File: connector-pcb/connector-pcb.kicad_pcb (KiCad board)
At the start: 2 copper layers, 79 x 43 mm, 39 parts, among them J1 MSO5000_LA, J2 IDC_HEADER_2x12, J3 IDC_HEADER_2x12, U1 MCP6002-xMS, U2 MCP6002-xMS

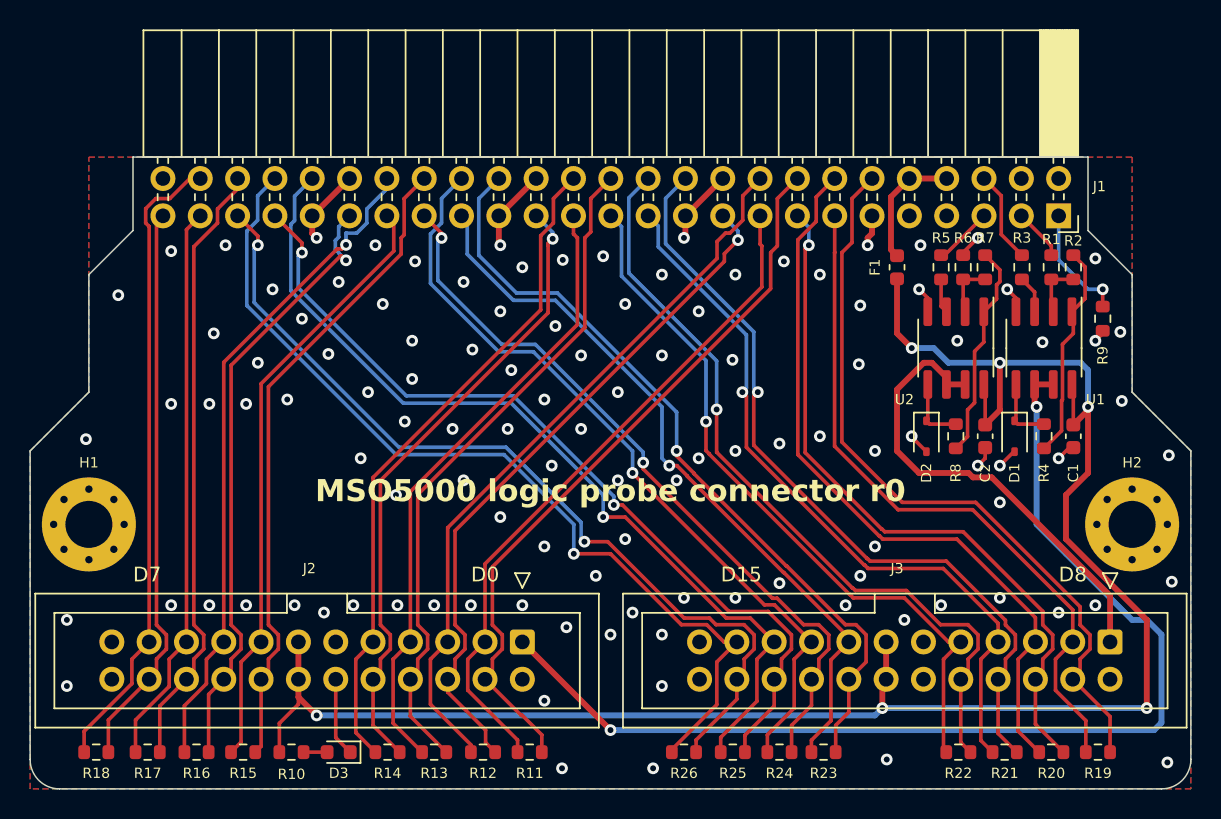
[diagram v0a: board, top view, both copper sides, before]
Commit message: Change connector PCB to 4 layer board, finalize probe board
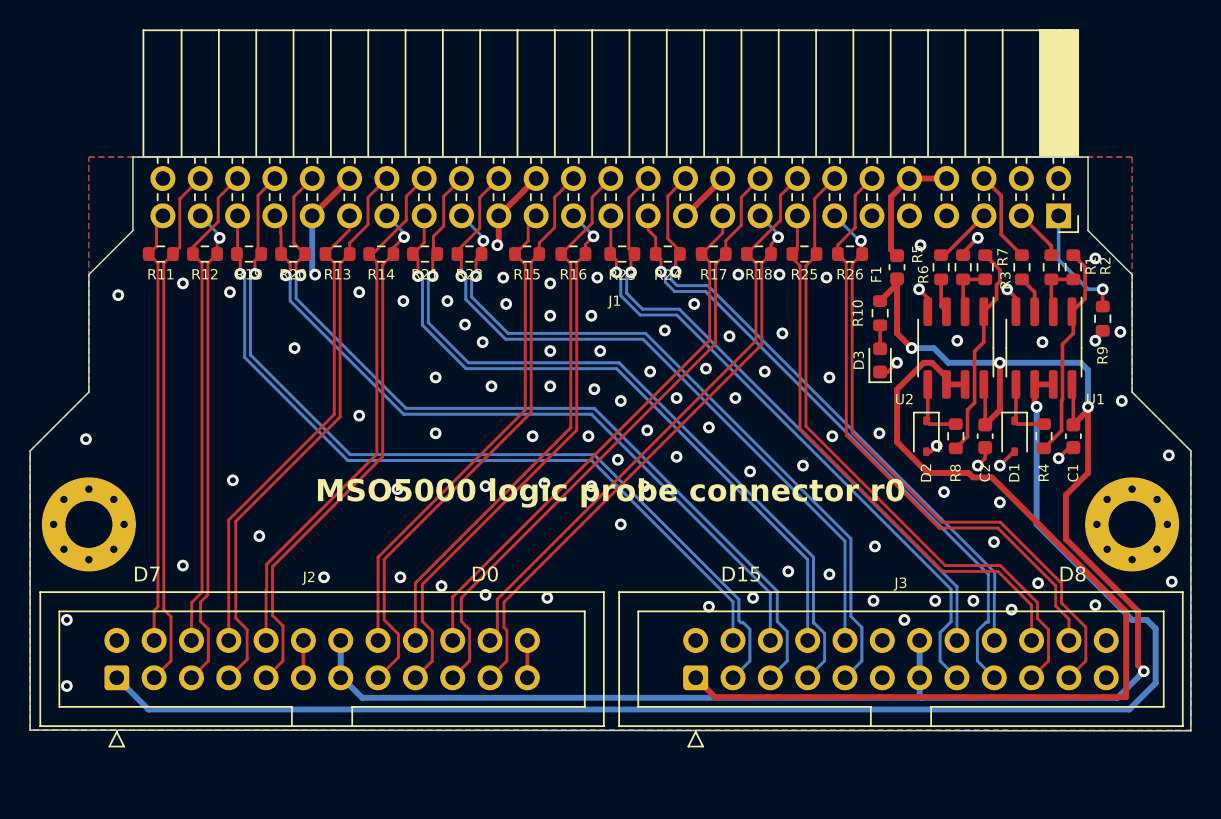
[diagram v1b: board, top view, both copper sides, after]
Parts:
- D1, D2: value 3.3V -> 3.3V 2%
- moved R19 67.0 mm to (74.9, 55.6), turned to 0 degrees
- moved R20 61.7 mm to (77.9, 55.6), turned to 0 degrees
- moved R18 56.4 mm to (109.6, 55.6), turned to 0 degrees
- moved R21 52.0 mm to (86.9, 55.6), turned to 0 degrees
- moved R17 51.3 mm to (106.5, 55.6), turned to 0 degrees
- moved R10 50.0 mm to (117.8, 59.6), turned to -90 degrees
- moved R22 47.5 mm to (89.9, 55.6), turned to 0 degrees
- moved D3 45.5 mm to (117.8, 62.8), turned to 90 degrees
- moved R16 42.5 mm to (97.0, 55.6), turned to 0 degrees
- moved R11 42.2 mm to (68.9, 55.6), turned to 0 degrees
- moved R15 39.0 mm to (93.8, 55.6), turned to 0 degrees
- moved R12 38.8 mm to (71.9, 55.6), turned to 0 degrees
- moved R23 36.6 mm to (100.3, 55.6)
- moved R26 35.7 mm to (115.8, 55.6), turned to 0 degrees
- moved R24 34.7 mm to (103.4, 55.6)
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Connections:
- J2 pad 10: /D3_N -> /D4_N
- J2 pad 15: /D4_P -> /D3_P
- J2 pad 16: /D4_N -> /D3_N
- J2 pad 17: /D5_P -> /D2_P
- J2 pad 18: /D5_N -> /D2_N
- J2 pad 19: /D6_P -> /D1_P
- J2 pad 20: /D6_N -> /D1_N
- J2 pad 21: /D7_P -> /D0_P
- J2 pad 22: /D7_N -> /D0_N
- J2 pad 3: /D0_P -> /D7_P
- J2 pad 4: /D0_N -> /D7_N
- J2 pad 5: /D1_P -> /D6_P
- J2 pad 6: /D1_N -> /D6_N
- J2 pad 7: /D2_P -> /D5_P
- J2 pad 8: /D2_N -> /D5_N
- J2 pad 9: /D3_P -> /D4_P
- J3 pad 10: /D11_N -> /D12_N
- J3 pad 15: /D12_P -> /D11_P
- J3 pad 16: /D12_N -> /D11_N
- J3 pad 17: /D13_P -> /D10_P
- J3 pad 18: /D13_N -> /D10_N
- J3 pad 19: /D14_P -> /D9_P
- J3 pad 20: /D14_N -> /D9_N
- J3 pad 21: /D15_P -> /D8_P
- J3 pad 22: /D15_N -> /D8_N
- J3 pad 3: /D8_P -> /D15_P
- J3 pad 4: /D8_N -> /D15_N
- J3 pad 5: /D9_P -> /D14_P
- J3 pad 6: /D9_N -> /D14_N
- J3 pad 7: /D10_P -> /D13_P
- J3 pad 8: /D10_N -> /D13_N
- J3 pad 9: /D11_P -> /D12_P
- R11 pad 1: /D0_N -> /D7_N
- R11 pad 2: /D0_P -> /D7_P
- R12 pad 1: /D1_N -> /D6_N
- R12 pad 2: /D1_P -> /D6_P
- R13 pad 1: /D2_N -> /D5_N
- R13 pad 2: /D2_P -> /D5_P
- R14 pad 1: /D3_N -> /D4_N
- R14 pad 2: /D3_P -> /D4_P
- R15 pad 1: /D4_N -> /D3_N
- R15 pad 2: /D4_P -> /D3_P
- R16 pad 1: /D5_N -> /D2_N
- R16 pad 2: /D5_P -> /D2_P
- R17 pad 1: /D6_N -> /D1_N
- R17 pad 2: /D6_P -> /D1_P
- R18 pad 1: /D7_N -> /D0_N
- R18 pad 2: /D7_P -> /D0_P
- R19 pad 1: /D8_N -> /D15_N
- R19 pad 2: /D8_P -> /D15_P
- R20 pad 1: /D9_N -> /D14_N
- R20 pad 2: /D9_P -> /D14_P
- R21 pad 1: /D10_N -> /D13_N
- R21 pad 2: /D10_P -> /D13_P
- R22 pad 1: /D11_N -> /D12_N
- R22 pad 2: /D11_P -> /D12_P
- R23 pad 1: /D12_N -> /D11_N
- R23 pad 2: /D12_P -> /D11_P
- R24 pad 1: /D13_N -> /D10_N
- R24 pad 2: /D13_P -> /D10_P
- R25 pad 1: /D14_N -> /D9_N
- R25 pad 2: /D14_P -> /D9_P
- R26 pad 1: /D15_N -> /D8_N
- R26 pad 2: /D15_P -> /D8_P
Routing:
- net /Vref_8_15_out: track 32.2 -> 65.9 mm
- net /Vref_0_7_out: track 74.6 -> 97.9 mm, vias 2 -> 1
- net /D10_N: track 53.8 -> 42.9 mm
- net +4V: track 127.8 -> 117.3 mm, vias 6 -> 4
- net /D9_N: track 48.3 -> 38.0 mm, vias 1 -> 0
- net /D11_N: track 53.3 -> 43.1 mm
- net /D8_N: track 51.4 -> 41.3 mm
- net /D1_N: track 47.0 -> 37.0 mm, vias 1 -> 0
- net /D5_N: track 42.3 -> 32.8 mm, vias 1 -> 0
- net /D0_N: track 50.1 -> 40.6 mm
- net /D3_N: track 43.3 -> 33.9 mm, vias 1 -> 0
- net /D7_N: track 38.6 -> 29.7 mm
- net /D2_N: track 46.3 -> 37.5 mm
- net /D6_N: track 41.8 -> 33.3 mm
- net /D14_N: track 58.8 -> 50.6 mm, vias 2 -> 1
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- added copper zone on In1.Cu, net GND
- added copper zone on In2.Cu, net GND
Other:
- board size 79 x 43 mm -> 79 x 39 mm
- copper layers 2 -> 4
- board text added: "Order selection:JLC7628, 1.6mm, 100Ohm diff. impedance"

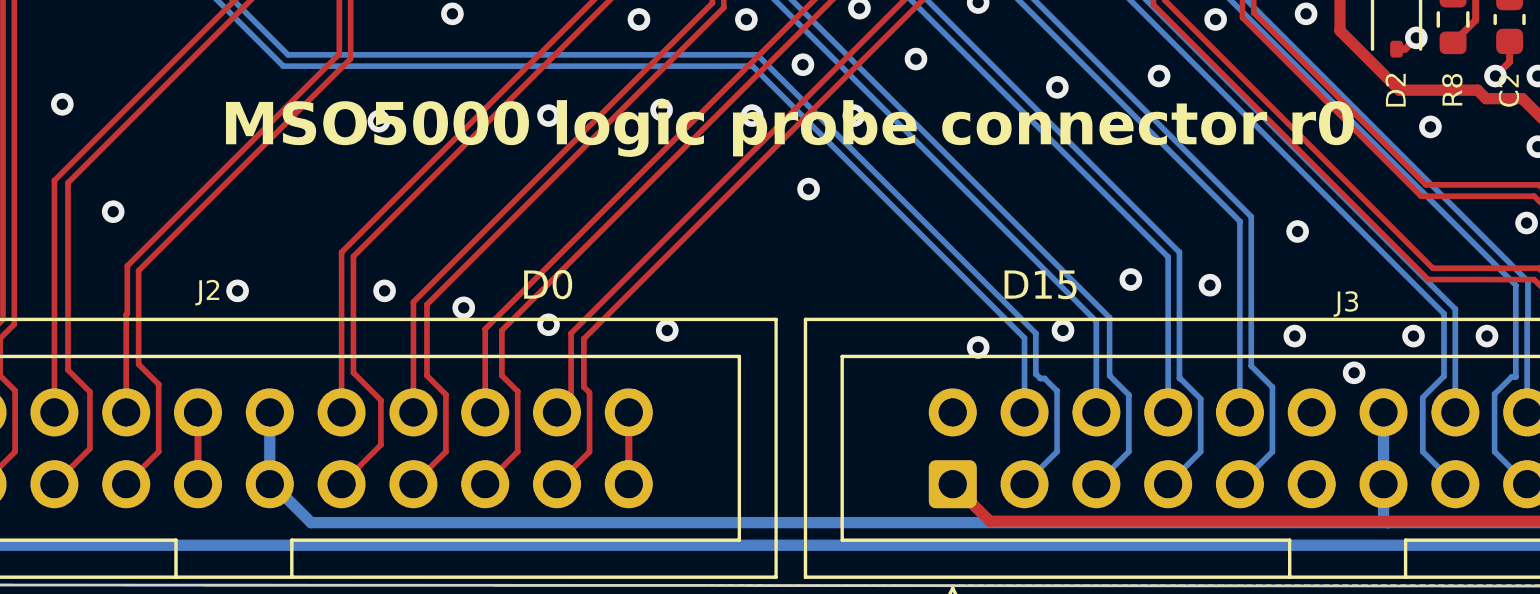
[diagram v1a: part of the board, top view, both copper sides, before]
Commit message: Add 3d model for 2x12 pin header (missing in kicad library), add readme
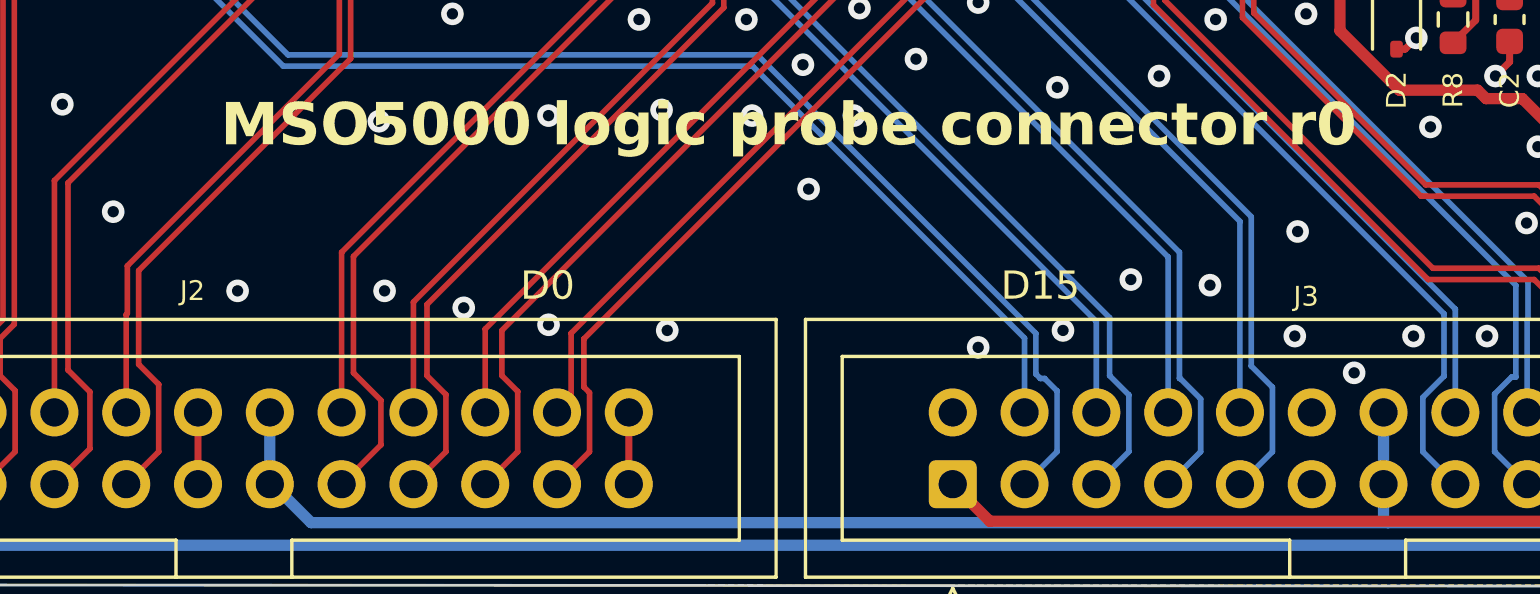
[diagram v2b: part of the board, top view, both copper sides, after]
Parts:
- J2, J3: footprint Connector_IDC:IDC-Header_2x12_P2.54mm_Vertical -> idc:IDC-Header_2x12_P2.54mm_Vertical
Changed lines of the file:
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@@
     (pad "20" thru_hole oval (at -2.54 22.86 270) (size 1.7 1.7) (drill 1) (layers "*.Cu" "*.Mask")
       (net 2 "GND") (pinfunction "GND") (pintype "passive"))
-    (pad "21" thru_hole oval locked (at 0 25.4 270) (size 1.7 1.7) (drill 1) (layers "*.Cu" "*.Mask")
+    (pad "21" thru_hole oval (at 0 25.4 270) (size 1.7 1.7) (drill 1) (layers "*.Cu" "*.Mask")
       (net 2 "GND") (pinfunction "GND") (pintype "passive"))
     (pad "22" thru_hole oval (at -2.54 25.4 270) (size 1.7 1.7) (drill 1) (layers "*.Cu" "*.Mask")
@@
     )
   )
-  (footprint "Connector_IDC:IDC-Header_2x12_P2.54mm_Vertical" (layer "F.Cu")
+  (footprint "idc:IDC-Header_2x12_P2.54mm_Vertical" (layer "F.Cu")
     (at 105.3 84.44 90)
     (descr "Through hole IDC box header, 2x12, 2.54mm pitch, DIN 41651 / IEC 60603-13, double rows, https://docs.google.com/spreadsheets/d/16SsEcesNF15N3Lb4niX7dcUr-NY5_MFPQhobNuNppn4/edit#gid=0")
@@
     (property "ki_keywords" "connector")
     (attr through_hole)
-    (fp_text reference "J3" (at 6.44 13.97) (layer "F.SilkS")
+    (fp_text reference "J3" (at 6.64 12.5 180) (layer "F.SilkS")
         (effects (font (size 0.7 0.7) (thickness 0.15)))
     )
@@
         (effects (font (size 1 1) (thickness 0.15)))
     )
-    (fp_text user "${REFERENCE}" (at 1.27 13.97) (layer "F.Fab")
+    (fp_text user "${REFERENCE}" (at 1.27 13.97 180) (layer "F.Fab")
         (effects (font (size 1 1) (thickness 0.15)))
     )
@@
     (pad "24" thru_hole circle (at 2.54 27.94 90) (size 1.7 1.7) (drill 1) (layers "*.Cu" "*.Mask")
       (net 2 "GND") (pinfunction "Pin_24") (pintype "passive"))
-    (model "${KICAD6_3DMODEL_DIR}/Connector_IDC.3dshapes/IDC-Header_2x12_P2.54mm_Vertical.wrl"
-      (offset (xyz 0 0 0))
-      (scale (xyz 1 1 1))
-      (rotate (xyz 0 0 0))
+    (model "${KIPRJMOD}/../idc.pretty/IDC_2x12.STEP"
+      (offset (xyz -3 5 0))
+      (scale (xyz 1 1 1))
+      (rotate (xyz -90 0 90))
     )
   )
@@
     )
   )
-  (footprint "Connector_IDC:IDC-Header_2x12_P2.54mm_Vertical" (layer "F.Cu")
+  (footprint "idc:IDC-Header_2x12_P2.54mm_Vertical" (layer "F.Cu")
     (at 65.9 84.44 90)
     (descr "Through hole IDC box header, 2x12, 2.54mm pitch, DIN 41651 / IEC 60603-13, double rows, https://docs.google.com/spreadsheets/d/16SsEcesNF15N3Lb4niX7dcUr-NY5_MFPQhobNuNppn4/edit#gid=0")
@@
     (property "ki_keywords" "connector")
     (attr through_hole)
-    (fp_text reference "J2" (at 6.84 13.1) (layer "F.SilkS")
+    (fp_text reference "J2" (at 6.84 12.5 180) (layer "F.SilkS")
         (effects (font (size 0.7 0.7) (thickness 0.15)))
     )
@@
         (effects (font (size 1 1) (thickness 0.15)))
     )
-    (fp_text user "${REFERENCE}" (at 1.27 13.97) (layer "F.Fab")
+    (fp_text user "${REFERENCE}" (at 1.27 13.97 180) (layer "F.Fab")
         (effects (font (size 1 1) (thickness 0.15)))
     )
@@
     (pad "24" thru_hole circle (at 2.54 27.94 90) (size 1.7 1.7) (drill 1) (layers "*.Cu" "*.Mask")
       (net 2 "GND") (pinfunction "Pin_24") (pintype "passive"))
-    (model "${KICAD6_3DMODEL_DIR}/Connector_IDC.3dshapes/IDC-Header_2x12_P2.54mm_Vertical.wrl"
-      (offset (xyz 0 0 0))
-      (scale (xyz 1 1 1))
-      (rotate (xyz 0 0 0))
-    )
-  )
+    (model "${KIPRJMOD}/../idc.pretty/IDC_2x12.STEP"
+      (offset (xyz -3 5 0))
+      (scale (xyz 1 1 1))
+      (rotate (xyz -90 0 90))
+    )
+  )

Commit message: Change zener diodes to 3.9V (should protect both 3.3V and 5V level shifters)
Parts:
- D1, D2: value 3.3V 2% -> 3.9V 5%
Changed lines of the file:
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@@
     (descr "SOD-323")
     (tags "SOD-323")
-    (property "LCSC#" "C116949")
-    (property "MPN" "MM3Z3V6T1G")
-    (property "Manufacturer" "onsemi")
+    (property "LCSC#" "C5359777")
+    (property "MPN" "MM3Z3V9")
+    (property "Manufacturer" "Fosan")
     (property "Sheetfile" "connector-pcb.kicad_sch")
     (property "Sheetname" "")
@@
         (effects (font (size 0.7 0.7) (thickness 0.15)))
     )
-    (fp_text value "3.3V 2%" (at 0.1 1.9 90) (layer "F.Fab")
+    (fp_text value "3.9V 5%" (at 0.1 1.9 90) (layer "F.Fab")
         (effects (font (size 1 1) (thickness 0.15)))
     )
@@
     (descr "SOD-323")
     (tags "SOD-323")
-    (property "LCSC#" "C116949")
-    (property "MPN" "MM3Z3V6T1G")
-    (property "Manufacturer" "onsemi")
+    (property "LCSC#" "C5359777")
+    (property "MPN" "MM3Z3V9")
+    (property "Manufacturer" "Fosan")
     (property "Sheetfile" "connector-pcb.kicad_sch")
     (property "Sheetname" "")
@@
         (effects (font (size 0.7 0.7) (thickness 0.15)))
     )
-    (fp_text value "3.3V 2%" (at 0.1 1.9 90) (layer "F.Fab")
-        (effects (font (size 1 1) (thickness 0.15)))
-    )
+    (fp_text value "3.9V 5%" (at 0.1 1.9 90) (layer "F.Fab")
+        (effects (font (size 1 1) (thickness 0.15)))
+    )

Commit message: Changed R9 of connector PCB from 10k to 100R (otherwise the scope wouldn't detect the probes)
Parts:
- R9: value 10K -> 100R
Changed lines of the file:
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@@
     (descr "Resistor SMD 0603 (1608 Metric), square (rectangular) end terminal, IPC_7351 nominal, (Body size source: IPC-SM-782 page 72, https://www.pcb-3d.com/wordpress/wp-content/uploads/ipc-sm-782a_amendment_1_and_2.pdf), generated with kicad-footprint-generator")
     (tags "resistor")
-    (property "LCSC#" "C98220")
-    (property "MPN" "RC0603FR-0710KL")
+    (property "LCSC#" "C105588")
+    (property "MPN" "RC0603FR-07100RL")
     (property "Manufacturer" "YAGEO")
     (property "Sheetfile" "connector-pcb.kicad_sch")
@@
         (effects (font (size 0.7 0.7) (thickness 0.15)))
     )
-    (fp_text value "10K" (at 0 1.43 90) (layer "F.Fab")
+    (fp_text value "100R" (at 0 1.43 90) (layer "F.Fab")
         (effects (font (size 1 1) (thickness 0.15)))
     )
